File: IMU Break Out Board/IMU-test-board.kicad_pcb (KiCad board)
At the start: 2 copper layers, 20 x 25 mm, 16 parts, among them J1 Conn_01x04, J2 Conn_01x03, U1 BMI088, U2 LSM6DSOTR, U3 LSM303AGRTR

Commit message: edits
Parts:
- added R3: 200, Resistor_SMD:R_0603_1608Metric, F.Cu at (56.7, 53.5)
- added REF**: TestPoint_Pad_D1.0mm, TestPoint:TestPoint_Pad_D1.0mm, F.Cu at (64.5, 54.5)
- D1: footprint LED_SMD:LED_0201_0603Metric -> LED_SMD:LED_0603_1608Metric
- moved D1 0.65 mm to (55.7, 56.7), turned to 90 degrees
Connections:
- D1 pad 2: +3.3V -> Net-(D1-A)
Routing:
- net +3.3V: track 56.7 -> 59.6 mm
- net Net-(D1-A): track 0.00 -> 2.48 mm
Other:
- outline, holes or cut-outs redrawn

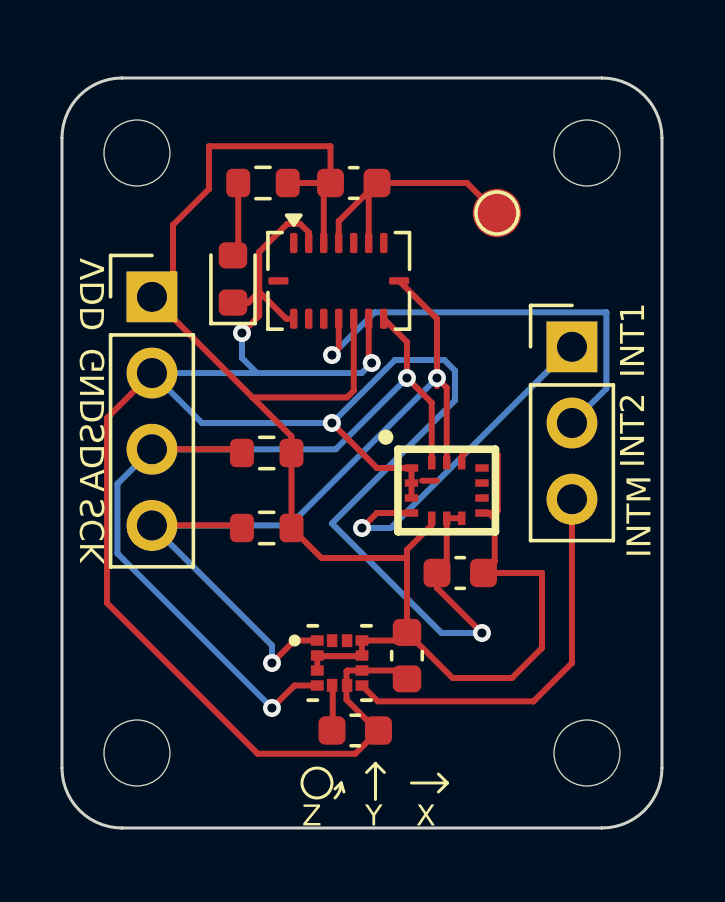
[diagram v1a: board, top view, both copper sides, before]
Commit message: Clean up IMU board and make it breadboard compatible
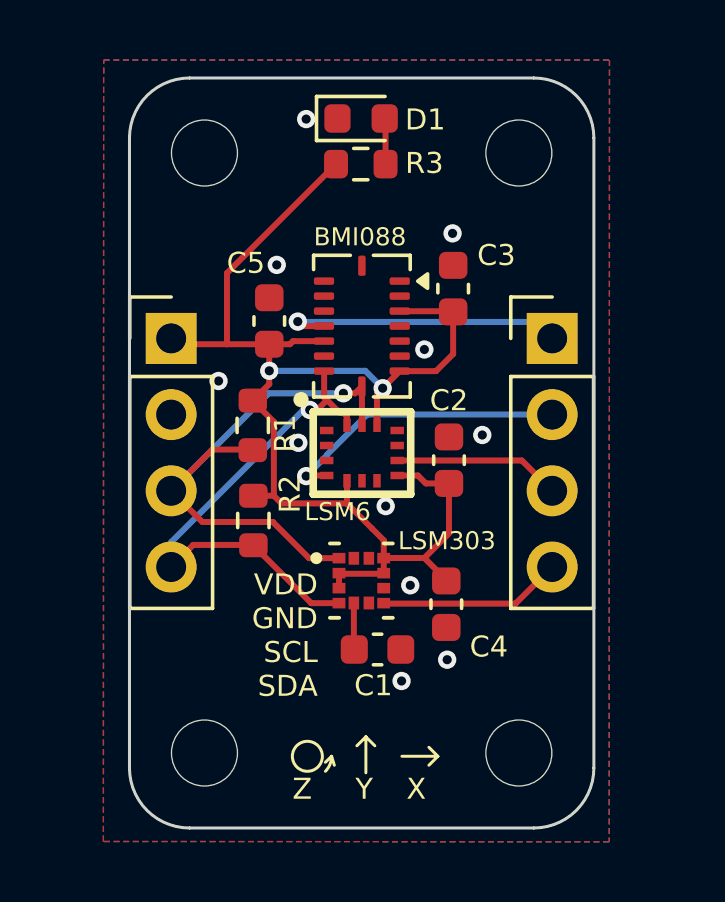
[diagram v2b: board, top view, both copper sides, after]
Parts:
- removed the REF** at (64.5, 54.5)
- added C5: .1uF, Capacitor_SMD:C_0603_1608Metric, F.Cu at (56.9, 58.1)
- D1: value LED -> GREEN
- J2: value Conn_01x03 -> Conn_01x04; footprint Connector_PinHeader_2.54mm:PinHeader_1x03_P2.54mm_Vertical -> Connector_PinHeader_2.54mm:PinHeader_1x04_P2.54mm_Vertical
- R3: value 200 -> 1k
- moved D1 6.85 mm to (60.0, 51.4), turned to 0 degrees
- moved C3 4.84 mm to (63.0, 57.0), turned to 90 degrees
- moved C2 3.78 mm to (62.9, 62.7), turned to 90 degrees
- moved R3 3.32 mm to (60.0, 52.9), turned to 0 degrees
- moved U2 3.09 mm to (60.0, 62.5)
- moved U3 2.84 mm to (60.0, 66.8)
- moved C1 2.80 mm to (60.5, 69.0)
- moved REF** 2.27 mm to (65.2, 72.5)
- moved REF** 2.27 mm to (65.2, 52.5)
- moved REF** 2.25 mm to (54.8, 52.5)
- moved REF** 2.25 mm to (54.8, 72.5)
- moved C4 2.16 mm to (62.8, 67.5)
- moved U1 1.69 mm to (60.0, 58.3), turned to -90 degrees
- moved J1 1.53 mm to (53.6, 58.7)
- moved R1 1.03 mm to (56.4, 61.6), turned to -90 degrees
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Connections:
- J1 pad 3: SDA -> SCL
- J1 pad 4: SCL -> SDA
- J2 pad 1: Int-Gyro1 -> Int-Gyro2
- J2 pad 2: Int-Gyro2 -> LSM6_INT1
- J2 pad 3: Int_Mag -> LSM6_INT2
- R1 pad 2: SDA -> SCL
- R2 pad 2: SCL -> SDA
- U2 pad 4: Int-Gyro1 -> LSM6_INT1
- U2 pad 9: unconnected-(U2-INT2-Pad9) -> LSM6_INT2
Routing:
- net GND: track 87.0 -> 0.00 mm, vias 4 -> 11
- net SDA: track 31.1 -> 16.9 mm, vias 2 -> 1
- net +3.3V: track 59.6 -> 45.6 mm, vias 0 -> 2
- net Int-Gyro1: track 11.4 -> 0.00 mm, vias 1 -> 0
- net SCL: track 29.6 -> 18.9 mm, vias 2 -> 1
- net LSM6_INT1: track 0.00 -> 9.75 mm, vias 0 -> 1
- net Int_Mag: track 13.2 -> 6.13 mm
- net LSM6_INT2: track 0.00 -> 5.58 mm
- net Int-Gyro2: track 15.2 -> 9.65 mm
- net Net-(D1-A): track 2.48 -> 1.57 mm
- added copper zone on B.Cu, net GND
- added copper zone on F.Cu, net GND
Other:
- board size 20 x 25 mm -> 15.5 x 25 mm
- board text added: "BMI088"
- board text added: "LSM303"
- board text added: "LSM6"
- board text added: "LSM6_1"
- board text added: "LSM6_2"
- board text added: "OwlSat Gyro/Mag Eval Board"
- board text added: "SCL"
- board text added: "VDD GND SCL SDA"
- board text removed: "INT1"
- board text removed: "INT2"
- board text removed: "INTM"
- board text removed: "SCK"
